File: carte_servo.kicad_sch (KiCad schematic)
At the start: 70 parts, among them J15 Conn_01x04_Pin, J16 Conn_01x05, J17 Conn_01x05, J2 Conn_02x04_Top_Bottom, J22 Conn_02x04_Top_Bottom, J23 Conn_01x05, J24 Conn_LEDs, SW1 SW_Reset, SW2 SW_Boot, U1 XGZP6897D_differential_pressu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

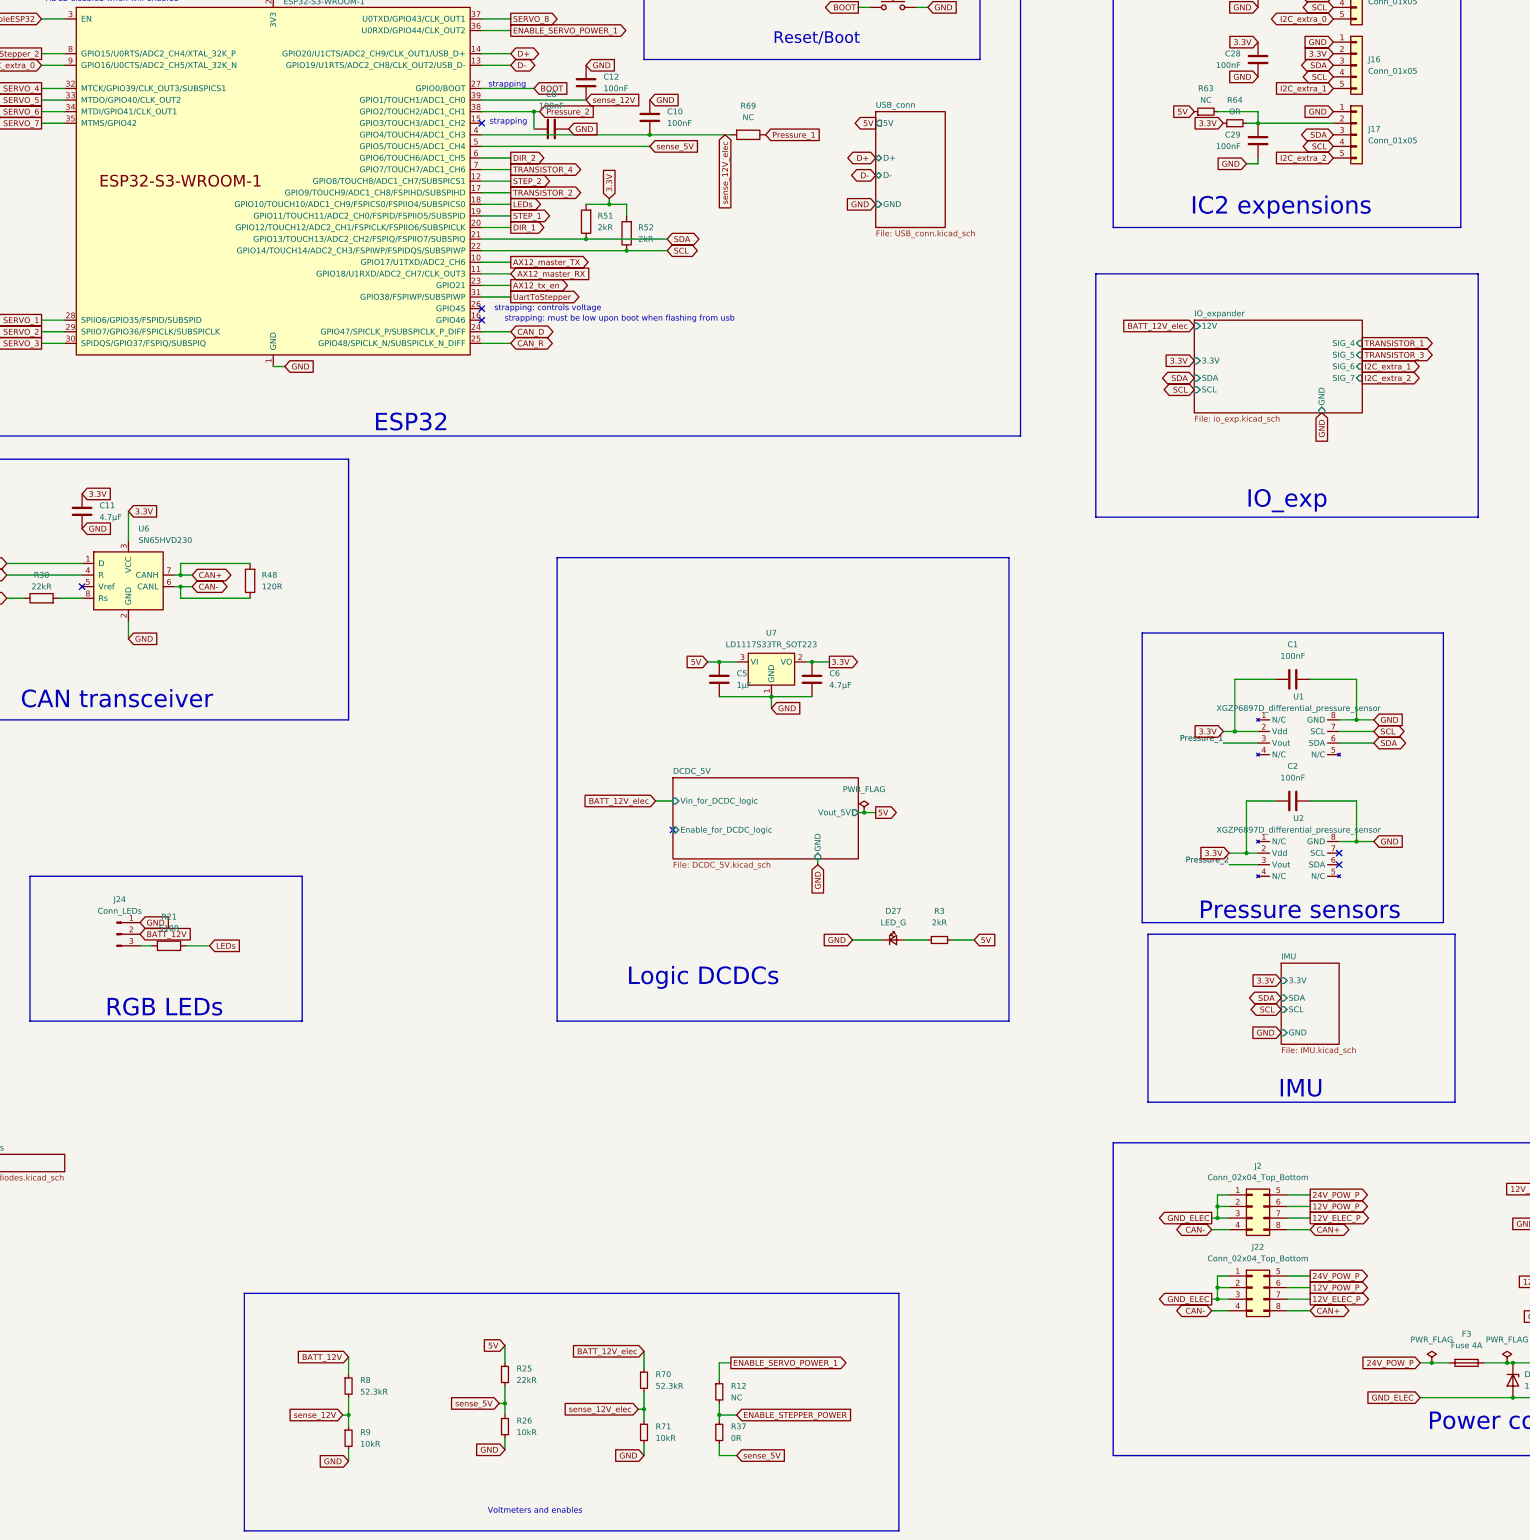
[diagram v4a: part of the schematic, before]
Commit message: add 24V monitoring, move transistor4 to IO_exp (former I2C extra 1)
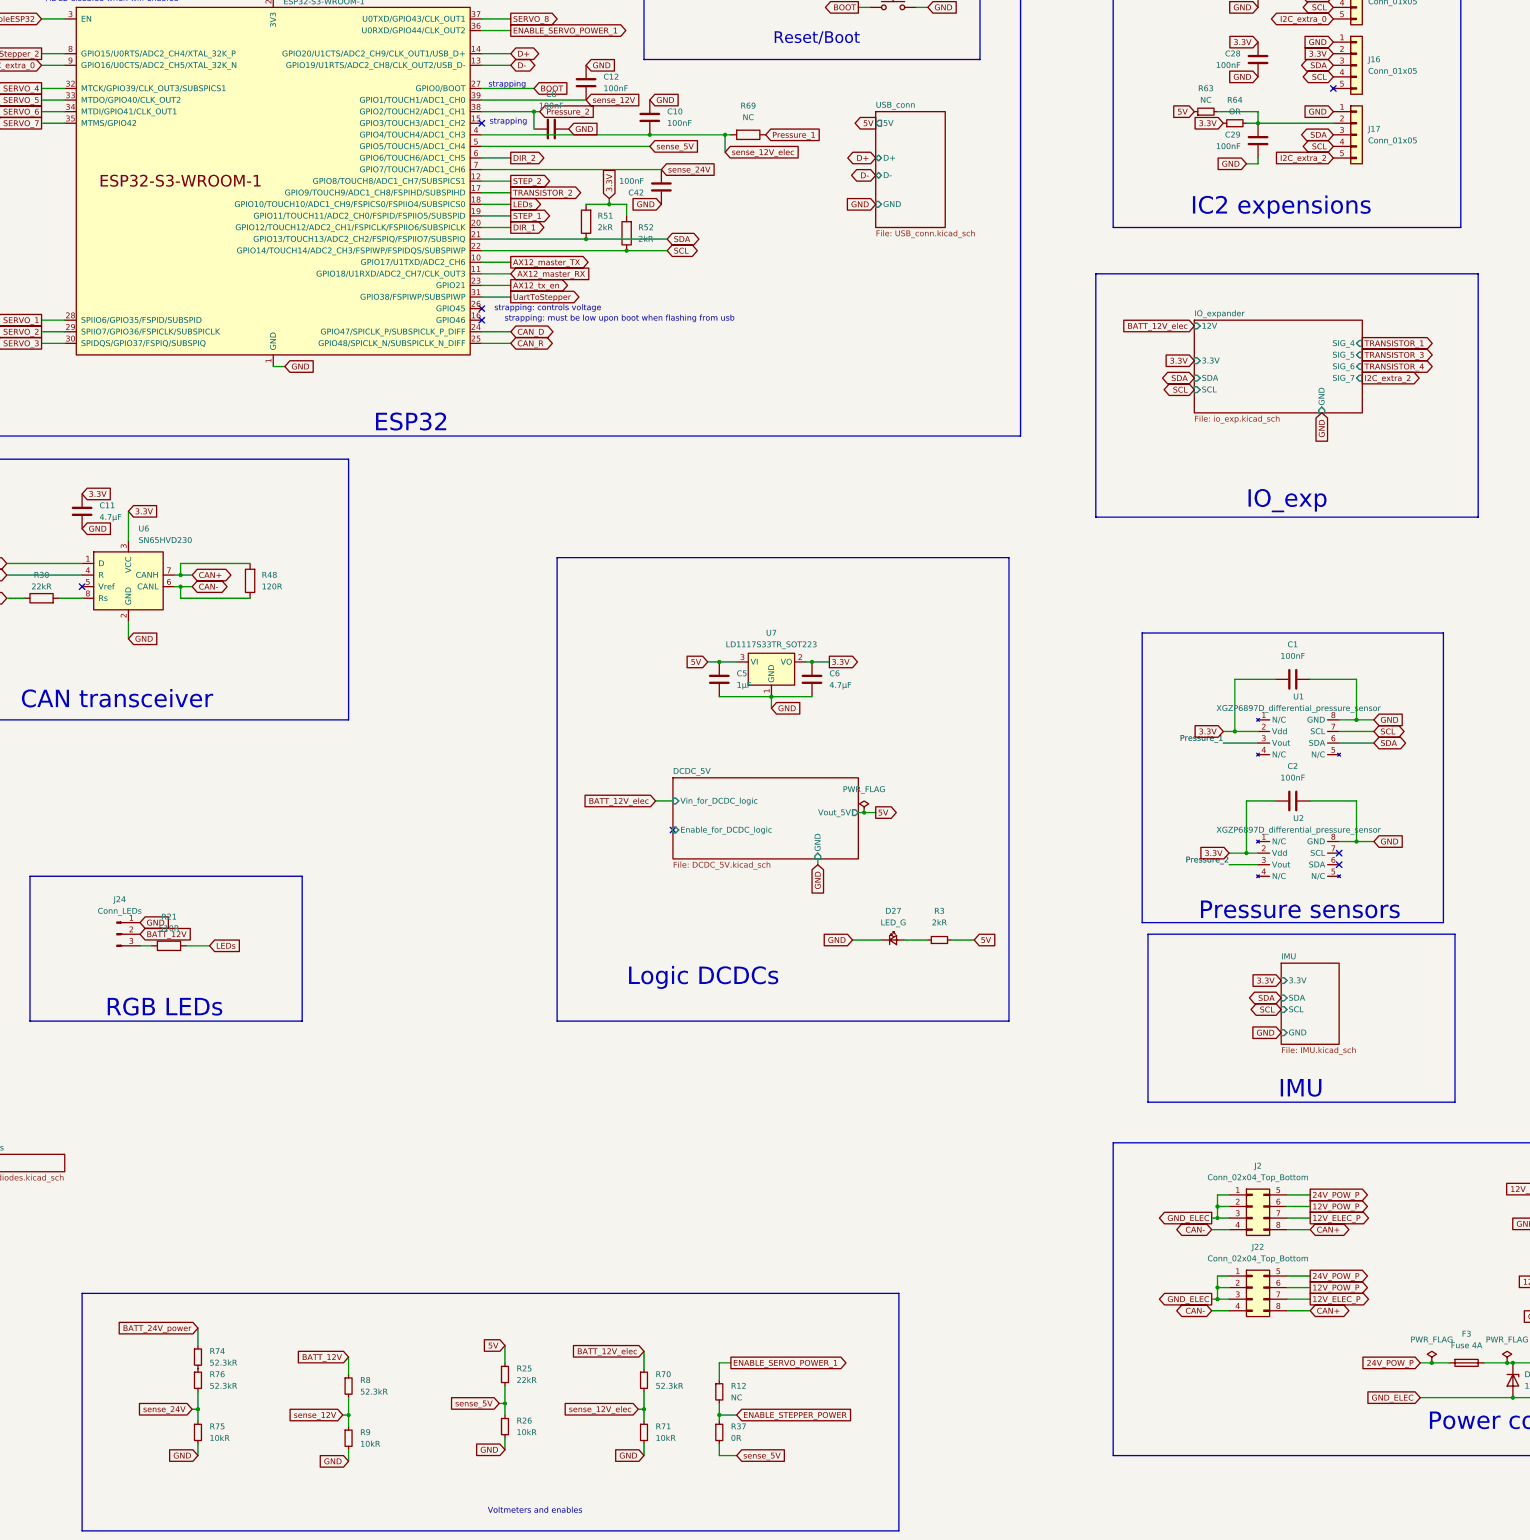
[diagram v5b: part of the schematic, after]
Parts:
- added C42: 100nF, Capacitor_SMD:C_0603_1608Metric, symbol Device:C
- added R74, R76: 52.3kR, Resistor_SMD:R_0603_1608Metric, symbol Device:R_Small
- added R75: 10kR, Resistor_SMD:R_0603_1608Metric, symbol Device:R_Small
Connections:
- net BATT_24V_power: now also R74.1
- net GND: now also C42.1, R75.2
- net TRANSISTOR_4: no longer U8.7 (GPIO7/TOUCH7/ADC1_CH6)
- net I2C_extra_1: no longer names the net of J16.5 (Pin_5)
- new net: R74.2, R76.1
- new net sense_24V: C42.2, R75.1, R76.2, U8.7 (GPIO7/TOUCH7/ADC1_CH6)
- no-connect marks 7 -> 8

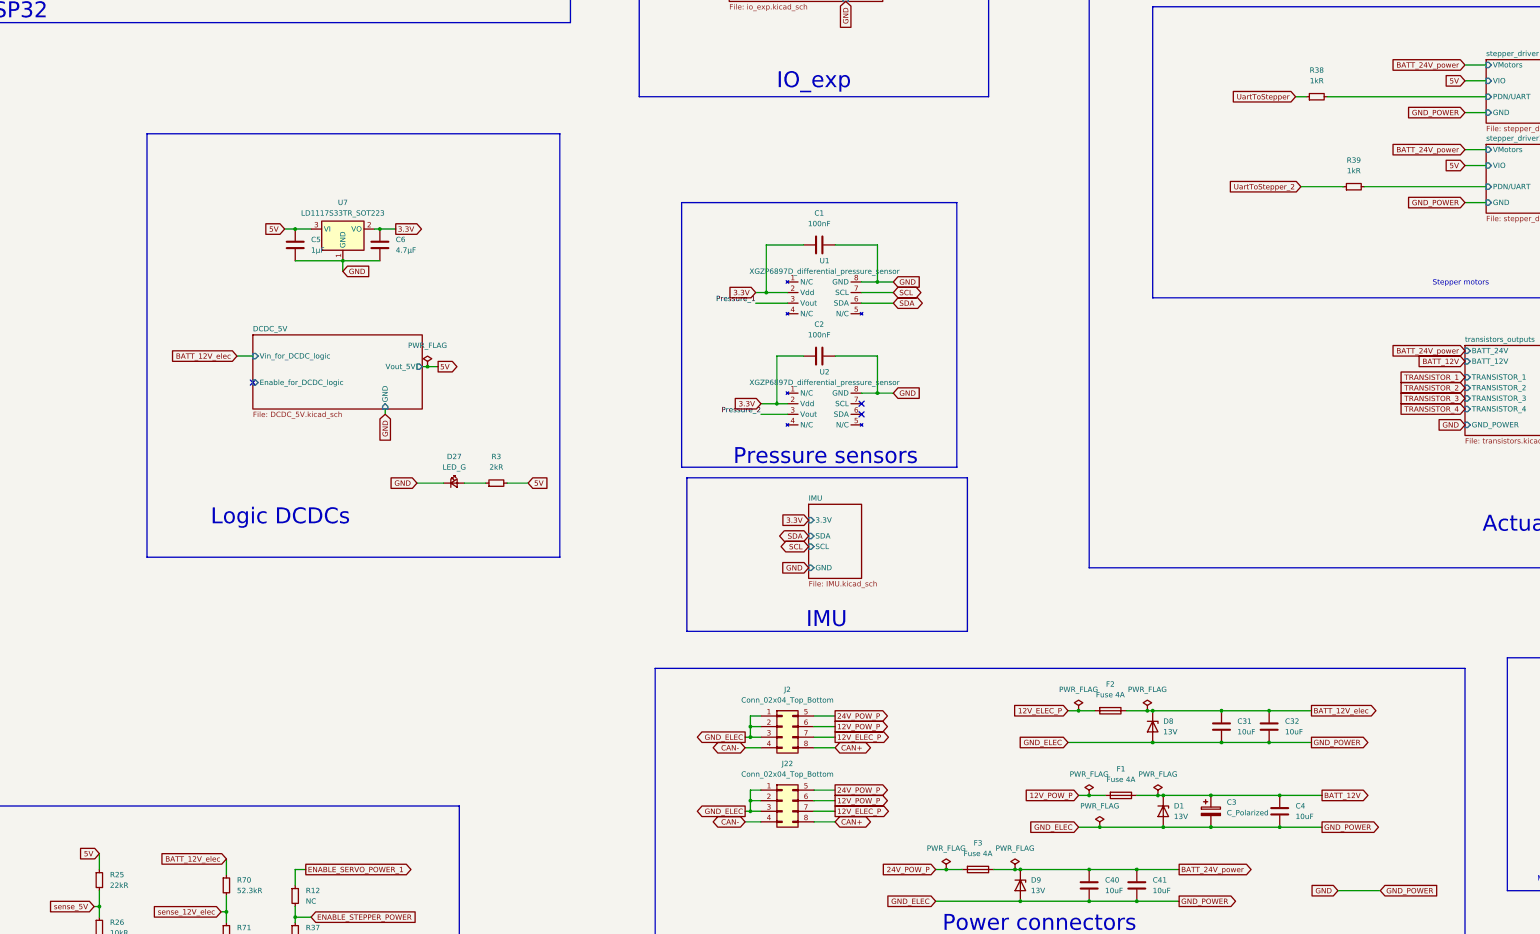
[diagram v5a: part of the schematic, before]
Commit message: 3.3V steppers
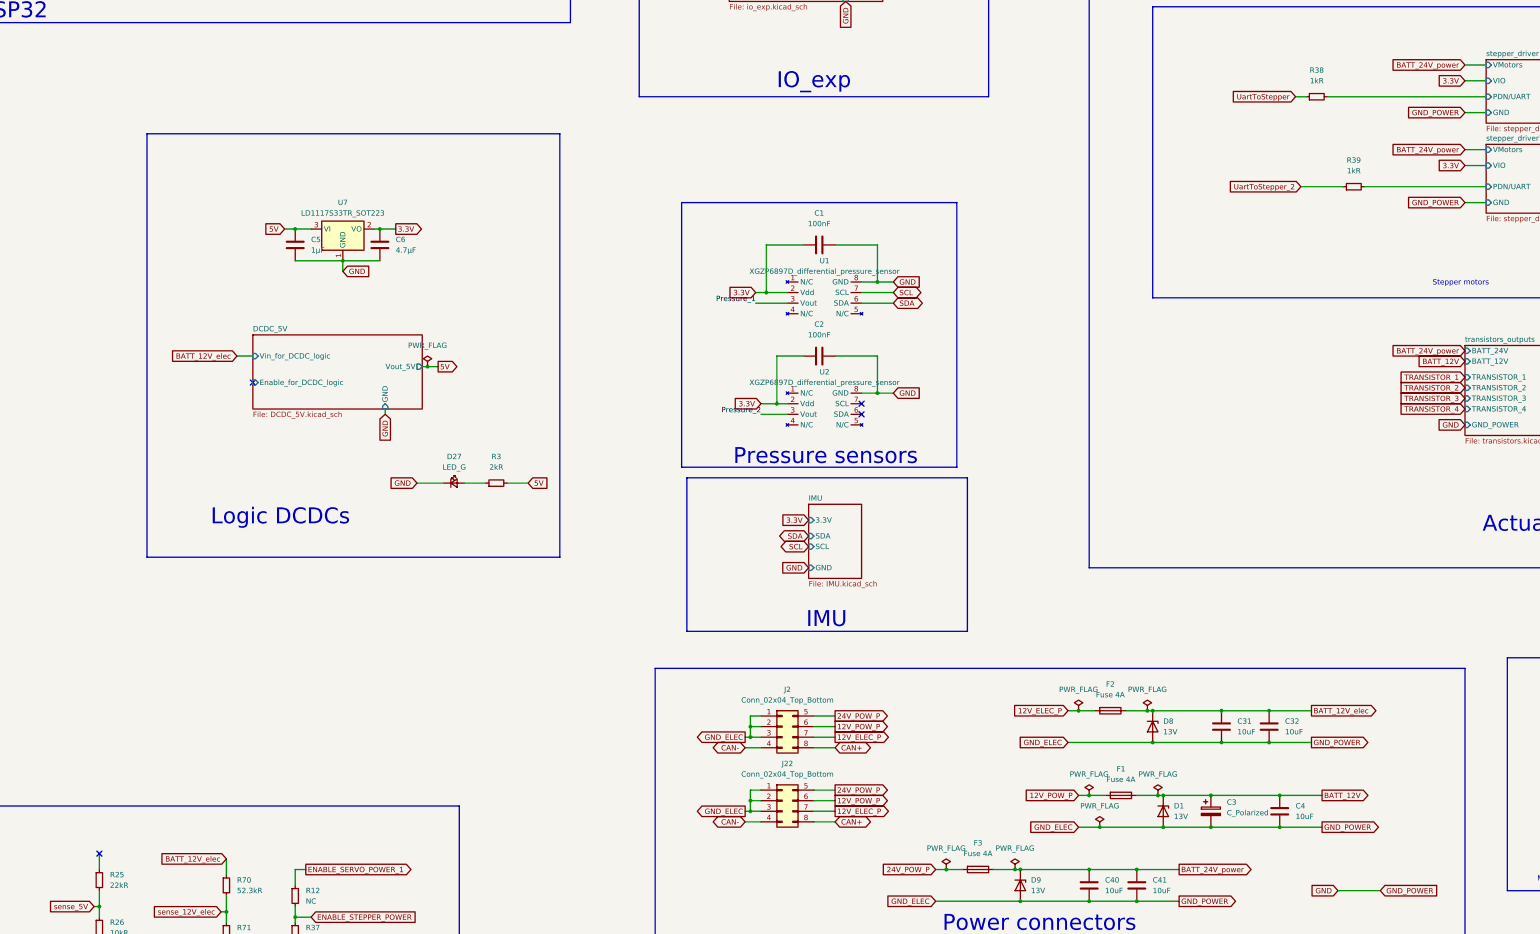
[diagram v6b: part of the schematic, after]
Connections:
- net 5V: no longer R25.1
- no-connect marks 8 -> 9
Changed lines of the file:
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@@
 	)
 	(no_connect
+		(at 146.05 342.9)
+	)
+	(no_connect
 		(at 140.97 115.57)
 	)
@@
 	(global_label "5V"
 		(shape input)
-		(at 473.71 177.8 180)
-		(fields_autoplaced yes)
-		(effects
-			(font
-				(size 1.27 1.27)
-			)
-			(justify right)
-		)
-		(property "Intersheetrefs" "${INTERSHEET_REFS}"
-			(at 468.9988 177.8794 0)
-			(effects
-				(font
-					(size 1.27 1.27)
-				)
-				(justify right)
-				(hide yes)
-			)
-		)
-	)
-	(global_label "5V"
-		(shape input)
 		(at 248.92 254 0)
 		(fields_autoplaced yes)
@@
 		)
 	)
-	(global_label "GND"
+	(global_label "3.3V"
 		(shape input)
-		(at 177.8 69.85 0)
+		(at 473.71 177.8 180)
 		(fields_autoplaced yes)
 		(effects
@@
 				(size 1.27 1.27)
 			)
-			(justify left)
+			(justify right)
 		)
 		(property "Intersheetrefs" "${INTERSHEET_REFS}"
-			(at 184.6557 69.85 0)
+			(at 466.6124 177.8 0)
 			(effects
 				(font
 					(size 1.27 1.27)
 				)
-				(justify left)
+				(justify right)
 				(hide yes)
 			)
@@
 	(global_label "GND"
 		(shape input)
-		(at 325.12 138.43 270)
+		(at 177.8 69.85 0)
 		(fields_autoplaced yes)
 		(effects
@@
 				(size 1.27 1.27)
 			)
-			(justify right)
+			(justify left)
 		)
 		(property "Intersheetrefs" "${INTERSHEET_REFS}"
-			(at 325.12 145.2857 90)
+			(at 184.6557 69.85 0)
 			(effects
 				(font
 					(size 1.27 1.27)
 				)
-				(justify right)
+				(justify left)
 				(hide yes)
 			)
@@
 	(global_label "GND"
 		(shape input)
-		(at 97.79 128.27 0)
+		(at 325.12 138.43 270)
 		(fields_autoplaced yes)
 		(effects
@@
 				(size 1.27 1.27)
 			)
-			(justify left)
+			(justify right)
 		)
 		(property "Intersheetrefs" "${INTERSHEET_REFS}"
-			(at 104.6457 128.27 0)
+			(at 325.12 145.2857 90)
 			(effects
 				(font
 					(size 1.27 1.27)
 				)
-				(justify left)
+				(justify right)
 				(hide yes)
 			)
 		)
 	)
-	(global_label "BATT_12V_elec"
+	(global_label "GND"
 		(shape input)
-		(at 176.53 344.17 180)
+		(at 97.79 128.27 0)
 		(fields_autoplaced yes)
 		(effects
@@
 				(size 1.27 1.27)
 			)
-			(justify right)
+			(justify left)
 		)
 		(property "Intersheetrefs" "${INTERSHEET_REFS}"
-			(at 159.8772 344.17 0)
+			(at 104.6457 128.27 0)
 			(effects
 				(font
 					(size 1.27 1.27)
 				)
-				(justify right)
+				(justify left)
 				(hide yes)
 			)
 		)
 	)
-	(global_label "5V"
+	(global_label "BATT_12V_elec"
 		(shape input)
-		(at 146.05 342.9 180)
+		(at 176.53 344.17 180)
 		(fields_autoplaced yes)
 		(effects
@@
 		)
 		(property "Intersheetrefs" "${INTERSHEET_REFS}"
-			(at 141.3388 342.8206 0)
+			(at 159.8772 344.17 0)
 			(effects
 				(font
@@
 		)
 	)
+	(global_label "3.3V"
+		(shape input)
+		(at 473.71 157.48 180)
+		(fields_autoplaced yes)
+		(effects
+			(font
+				(size 1.27 1.27)
+			)
+			(justify right)
+		)
+		(property "Intersheetrefs" "${INTERSHEET_REFS}"
+			(at 466.6124 157.48 0)
+			(effects
+				(font
+					(size 1.27 1.27)
+				)
+				(justify right)
+				(hide yes)
+			)
+		)
+	)
 	(global_label "CAN_R"
 		(shape bidirectional)
@@
 				(hide yes)
 			)
-		)
-	)
-	(global_label "5V"
-		(shape input)
-		(at 473.71 157.48 180)
-		(fields_autoplaced yes)
-		(effects
-			(font
-				(size 1.27 1.27)
-			)
-			(justify right)
-		)
-		(property "Intersheetrefs" "${INTERSHEET_REFS}"
-			(at 468.9988 157.5594 0)
-			(effects
-				(font
-					(size 1.27 1.27)
-				)
-				(justify right)
-				(hide yes)
-			)

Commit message: update to Kicad 9 + small fixes
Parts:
- removed R12: NC, Resistor_SMD:R_0603_1608Metric, symbol Device:R_Small
- removed R25: 22kR, Resistor_SMD:R_0603_1608Metric, symbol Device:R_Small
- removed R26: 10kR, Resistor_SMD:R_0603_1608Metric, symbol Device:R_Small
- removed R37: 0R, Resistor_SMD:R_0603_1608Metric, symbol Device:R_Small
- added R77: 0R_S2u2, Resistor_SMD:R_0603_1608Metric, symbol Device:R
- added R78: 0R_S2u, Resistor_SMD:R_0603_1608Metric, symbol Device:R
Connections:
- net sense_5V is gone; now on net ENABLE_STEPPER_POWER: U8.5 (GPIO5/TOUCH5/ADC1_CH4)
- net DIR_2: now also U8.9 (GPIO16/U0CTS/ADC2_CH5/XTAL_32K_N); no longer U8.6 (GPIO6/TOUCH6/ADC1_CH5)
- net I2C_extra_0: now also U8.6 (GPIO6/TOUCH6/ADC1_CH5); no longer U8.9 (GPIO16/U0CTS/ADC2_CH5/XTAL_32K_N)
- net SERVO_7: now also R77.2
- net SERVO_8: now also R78.2
- net stepper_driver/PDN/UART renamed StepperToUart
- net StepperToUart: now also R78.1
- net stepper_driver1/PDN/UART renamed StepperToUart_2
- net StepperToUart_2: now also R77.1
- no-connect marks 9 -> 8
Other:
- note added: "When using Octal flash or Octal PSRAM or both, GPIO33 ~ GPIO37 are used internally"
- moved on the sheet: R38, R39, R70, R71
